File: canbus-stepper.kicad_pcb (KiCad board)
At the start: 2 copper layers, 40.3 x 40.3 mm, 64 parts, among them J1 TYPE-C USB SOCKET, J2 Motor Output, J3 CAN Daisy-Chain 1, J4 CAN Daisy-Chain 2, J5 Qwiic I2C, J6 AUX Port, J7 SFV30R-2STBE1HLF (30-Pin OLED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, J8 24V Power Input Terminal, J9 24V Power Output Terminal, Q1 AO4407A, SW1 SW_Push, SW2 SW_Push, SW3 SW_Push, SW4 SW_Push, U1 ESP32-S3-WROOM-1, U2 TMC2209, U3 AS5600-ASOT, U4 TCAN1051VDRBTQ1, U5 MP2315, U6 AP2112K-3.3TRG1, U7 USBLC6-2SC6

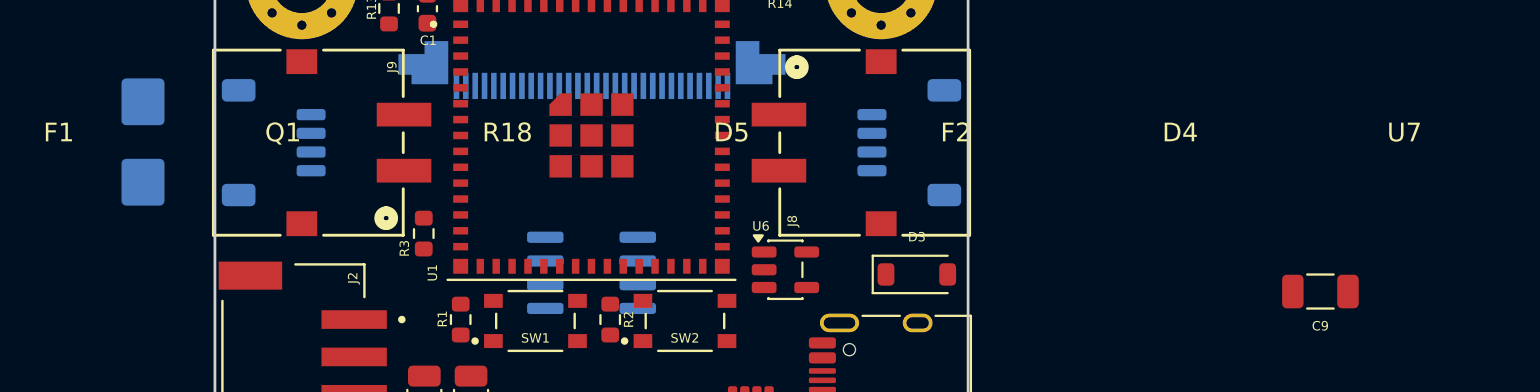
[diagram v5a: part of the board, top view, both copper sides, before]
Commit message: fix: embed graphical symbol definitions in lib_symbols for F1, F2, Q1, D4, D5, U7 to eliminate question mark boxes
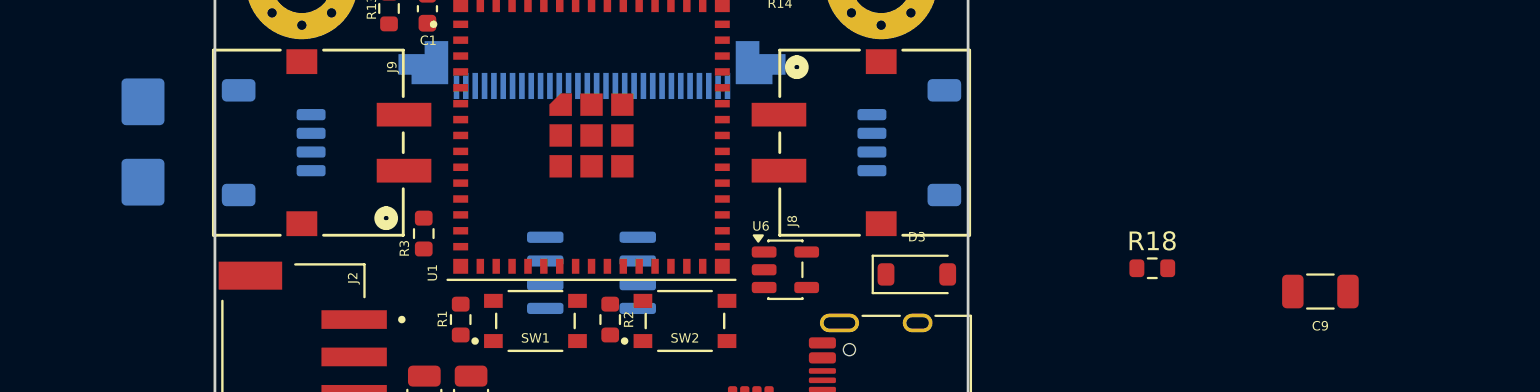
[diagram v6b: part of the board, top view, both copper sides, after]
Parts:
- removed D4: PESD1CAN, Package_TO_SOT_SMD:SOT-23
- removed D5: BZX84C12V, Diode_SMD:D_SOT-23_ANK
- removed F1: 3.5A 30V PPTC, Fuse:Fuse_1812_4532Metric
- removed F2: 500mA 16V PPTC, Fuse:Fuse_0805_2012Metric
- removed Q1: AO4407A, Package_SO:SOIC-8_3.9x4.9mm_P1.27mm
- removed U7: USBLC6-2SC6, Package_TO_SOT_SMD:SOT-23-6
- moved R18 34.8 mm to (178.5, 104.8)

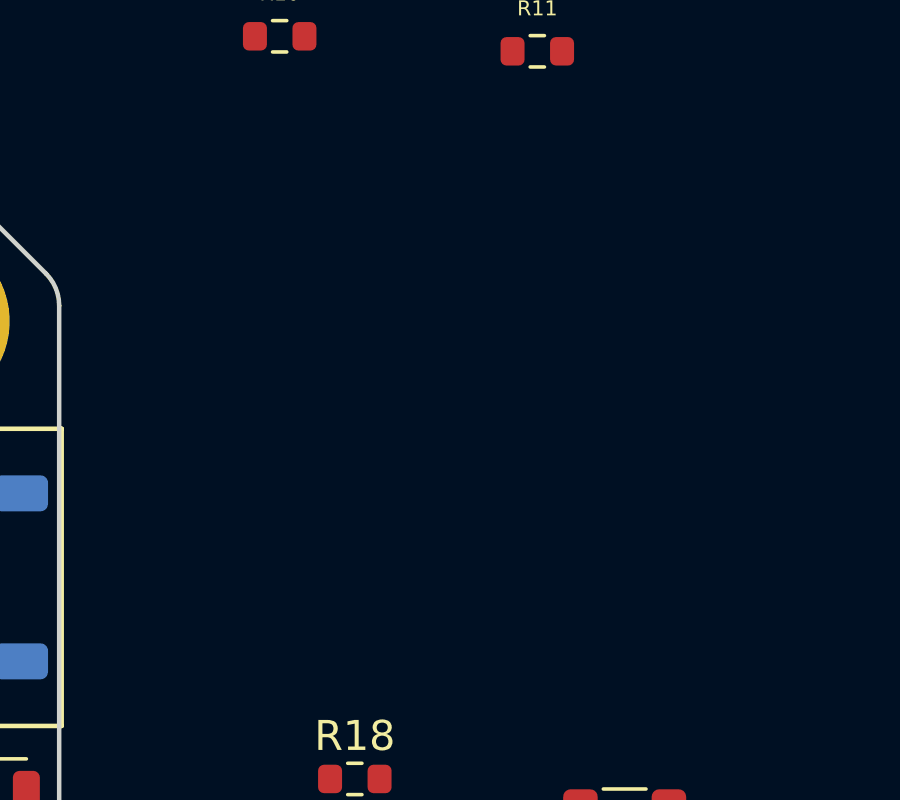
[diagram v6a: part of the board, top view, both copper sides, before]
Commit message: fix: resolve D5 footprint name to Package_TO_SOT_SMD:SOT-23, map Q1 SOIC-8 8-pins, and add pin UUID instances
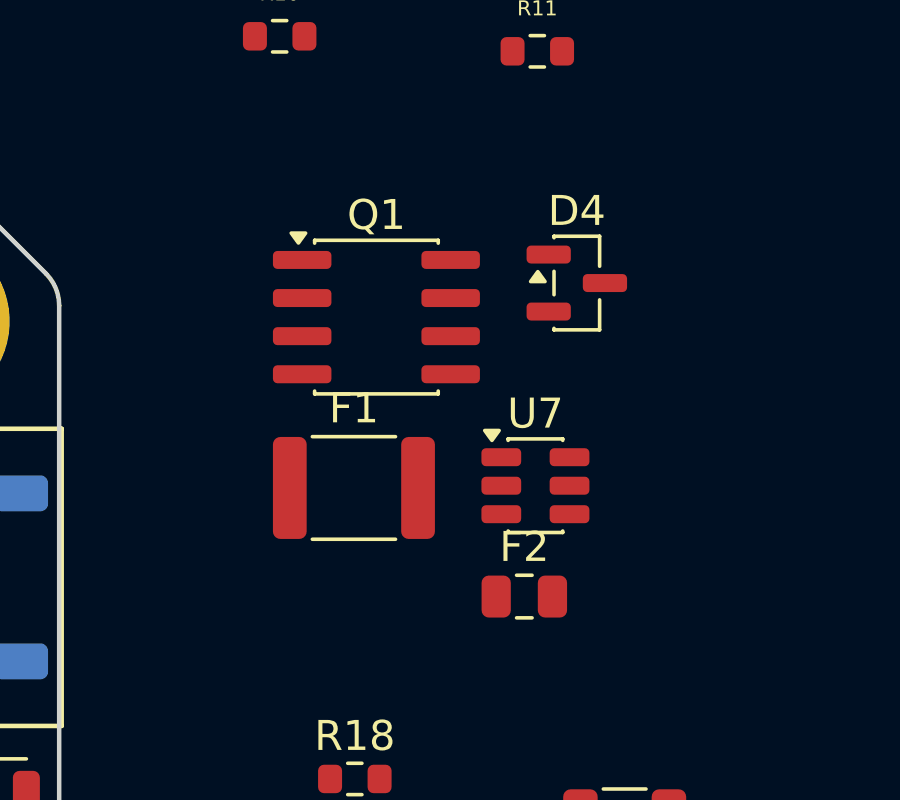
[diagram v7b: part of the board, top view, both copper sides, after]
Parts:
- added D4: PESD1CAN, Package_TO_SOT_SMD:SOT-23, F.Cu at (185.9, 88.2)
- added F1: 3.5A 30V PPTC, Fuse:Fuse_1812_4532Metric, F.Cu at (178.5, 95.1)
- added F2: 500mA 16V PPTC, Fuse:Fuse_0805_2012Metric, F.Cu at (184.2, 98.7)
- added Q1: AO4407A, Package_SO:SOIC-8_3.9x4.9mm_P1.27mm, F.Cu at (179.2, 89.4)
- added U7: USBLC6-2SC6, Package_TO_SOT_SMD:SOT-23-6, F.Cu at (184.5, 95.0)

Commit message: chore: save PCB editor update state prior to unplaced component grouping
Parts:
- added D5: BZX84C12V, Package_TO_SOT_SMD:SOT-23, F.Cu at (199.2, 92.0)
- moved C9 9.15 mm to (196.6, 105.9)
- moved R18 8.65 mm to (187.1, 104.2)
- moved D4 8.24 mm to (194.1, 88.8)
- moved F2 7.94 mm to (191.0, 102.7)
- moved R11 7.87 mm to (192.4, 81.3)
- moved C11 6.46 mm to (210.1, 124.3)
- moved U7 6.01 mm to (189.0, 99.0)
- moved F1 5.95 mm to (184.4, 95.4)
- moved C14 5.82 mm to (213.8, 113.8)
- moved R8 5.77 mm to (203.4, 101.3)
- moved C8 5.64 mm to (208.8, 112.5)
- moved C7 4.93 mm to (207.6, 108.8)
- moved Q1 4.76 mm to (179.5, 84.6)
- moved C15 4.61 mm to (212.6, 118.8)
- moved R7 4.23 mm to (217.6, 107.5)
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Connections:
- Q1 pad 4: (no net) -> unconnected-(Q1-G-Pad4)
- Q1 pad 5: (no net) -> unconnected-(Q1-D-Pad5)
- Q1 pad 6: (no net) -> unconnected-(Q1-D-Pad6)
- Q1 pad 7: (no net) -> unconnected-(Q1-D-Pad7)
- Q1 pad 8: (no net) -> unconnected-(Q1-D-Pad8)
